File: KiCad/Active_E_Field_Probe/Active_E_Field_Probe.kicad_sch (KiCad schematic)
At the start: 8 parts

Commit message: Something
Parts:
- removed D1: ~, symbol SLiCAP:D
- removed G1: 0.5*s*{C_s}, symbol SLiCAP:G
- removed G2: 2.5*s*{C_s}, symbol SLiCAP:G
- removed H1: 5, symbol SLiCAP:H
- added C1: {0.5*C_s}, symbol SLiCAP:C
- added R1: 50, symbol SLiCAP:R
- R2: noisetemp 0 -> 343
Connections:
- net 0: now also N1.2 (outN)
- net at N1.1 (outP): now also C1.2, R1.1; no longer R2.1
- net at C2.2, N1.3 (inp): now also C1.1
- new net out: R1.2, R2.1
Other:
- moved on the sheet: C2, N1, R2, V1

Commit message: continued work on brute force
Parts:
- R1, R2: noisetemp 343 -> {T_op_max}
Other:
- moved on the sheet: C1, N1
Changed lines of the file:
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@@
 	)
 	(junction
-		(at 123.19 78.74)
+		(at 115.57 78.74)
 		(diameter 0)
 		(color 0 0 0 0)
 	)
 	(junction
-		(at 129.54 78.74)
+		(at 121.92 78.74)
 		(diameter 0)
 		(color 0 0 0 0)
 	)
 	(junction
-		(at 120.65 58.42)
+		(at 113.03 58.42)
 		(diameter 0)
 		(color 0 0 0 0)
 	)
 	(junction
-		(at 130.81 58.42)
+		(at 123.19 58.42)
 		(diameter 0)
 		(color 0 0 0 0)
@@
 	(wire
 		(pts
-			(xy 129.54 73.66) (xy 129.54 78.74)
-		)
-		(stroke
-			(width 0)
-			(type default)
-		)
-	)
-	(wire
-		(pts
-			(xy 120.65 58.42) (xy 123.19 58.42)
-		)
-		(stroke
-			(width 0)
-			(type default)
-		)
-	)
-	(wire
-		(pts
-			(xy 120.65 53.34) (xy 120.65 58.42)
-		)
-		(stroke
-			(width 0)
-			(type default)
-		)
-	)
-	(wire
-		(pts
-			(xy 80.01 78.74) (xy 123.19 78.74)
+			(xy 121.92 73.66) (xy 121.92 78.74)
+		)
+		(stroke
+			(width 0)
+			(type default)
+		)
+	)
+	(wire
+		(pts
+			(xy 113.03 58.42) (xy 115.57 58.42)
+		)
+		(stroke
+			(width 0)
+			(type default)
+		)
+	)
+	(wire
+		(pts
+			(xy 113.03 53.34) (xy 113.03 58.42)
+		)
+		(stroke
+			(width 0)
+			(type default)
+		)
+	)
+	(wire
+		(pts
+			(xy 80.01 78.74) (xy 115.57 78.74)
 		)
 		(stroke
@@
 	(wire
 		(pts
-			(xy 123.19 78.74) (xy 123.19 81.28)
+			(xy 115.57 78.74) (xy 115.57 81.28)
 		)
 		(stroke
@@
 	(wire
 		(pts
-			(xy 130.81 53.34) (xy 130.81 58.42)
+			(xy 123.19 53.34) (xy 123.19 58.42)
 		)
 		(stroke
@@
 	(wire
 		(pts
-			(xy 130.81 58.42) (xy 134.62 58.42)
-		)
-		(stroke
-			(width 0)
-			(type default)
-		)
-	)
-	(wire
-		(pts
-			(xy 80.01 58.42) (xy 120.65 58.42)
+			(xy 123.19 58.42) (xy 134.62 58.42)
+		)
+		(stroke
+			(width 0)
+			(type default)
+		)
+	)
+	(wire
+		(pts
+			(xy 80.01 58.42) (xy 113.03 58.42)
 		)
 		(stroke
@@
 	(wire
 		(pts
-			(xy 129.54 58.42) (xy 130.81 58.42)
+			(xy 121.92 58.42) (xy 123.19 58.42)
 		)
 		(stroke
@@
 	(wire
 		(pts
-			(xy 123.19 63.5) (xy 123.19 58.42)
+			(xy 115.57 63.5) (xy 115.57 58.42)
 		)
 		(stroke
@@
 	(wire
 		(pts
-			(xy 123.19 73.66) (xy 123.19 78.74)
+			(xy 115.57 73.66) (xy 115.57 78.74)
 		)
 		(stroke
@@
 	(wire
 		(pts
-			(xy 129.54 78.74) (xy 148.59 78.74)
-		)
-		(stroke
-			(width 0)
-			(type default)
-		)
-	)
-	(wire
-		(pts
-			(xy 123.19 78.74) (xy 129.54 78.74)
-		)
-		(stroke
-			(width 0)
-			(type default)
-		)
-	)
-	(wire
-		(pts
-			(xy 129.54 58.42) (xy 129.54 63.5)
+			(xy 121.92 78.74) (xy 148.59 78.74)
+		)
+		(stroke
+			(width 0)
+			(type default)
+		)
+	)
+	(wire
+		(pts
+			(xy 115.57 78.74) (xy 121.92 78.74)
+		)
+		(stroke
+			(width 0)
+			(type default)
+		)
+	)
+	(wire
+		(pts
+			(xy 121.92 58.42) (xy 121.92 63.5)
 		)
 		(stroke
@@
 			)
 		)
-		(property "noisetemp" "343"
+		(property "noisetemp" "{T_op_max}"
 			(at 139.7 46.99 90)
 			(show_name yes)
@@
 			)
 		)
-		(property "noisetemp" "343"
+		(property "noisetemp" "{T_op_max}"
 			(at 151.13 67.3099 0)
 			(show_name yes)
@@
 	(symbol
 		(lib_id "SLiCAP:N")
-		(at 129.54 68.58 0)
+		(at 121.92 68.58 0)
 		(unit 1)
 		(exclude_from_sim no)
@@
 		(fields_autoplaced yes)
 		(property "Reference" "N1"
-			(at 132.08 68.5798 0)
+			(at 124.46 68.5798 0)
 			(effects
 				(font
@@
 		)
 		(property "Value" "~"
-			(at 135.89 69.215 0)
+			(at 128.27 69.215 0)
 			(effects
 				(font
@@
 		)
 		(property "Footprint" ""
-			(at 129.54 69.85 0)
+			(at 121.92 69.85 0)
 			(effects
 				(font
@@
 		)
 		(property "Datasheet" ""
-			(at 129.54 69.85 0)
+			(at 121.92 69.85 0)
 			(effects
 				(font
@@
 		)
 		(property "Description" "Nullor"
-			(at 134.62 72.644 0)
+			(at 127 72.644 0)
 			(effects
 				(font
@@
 		)
 		(property "model" "N"
-			(at 131.445 70.485 0)
+			(at 123.825 70.485 0)
 			(show_name yes)
 			(effects
@@
 	(symbol
 		(lib_id "SLiCAP:GND")
-		(at 123.19 81.28 0)
+		(at 115.57 81.28 0)
 		(unit 1)
 		(exclude_from_sim no)
@@
 		(fields_autoplaced yes)
 		(property "Reference" "#01"
-			(at 123.19 86.36 0)
+			(at 115.57 86.36 0)
 			(effects
 				(font
@@
 		)
 		(property "Value" "0"
-			(at 123.19 83.82 0)
+			(at 115.57 83.82 0)
 			(do_not_autoplace yes)
 			(effects
@@
 		)
 		(property "Footprint" ""
-			(at 123.19 81.28 0)
+			(at 115.57 81.28 0)
 			(effects
 				(font
@@
 		)
 		(property "Datasheet" ""
-			(at 123.19 91.44 0)
+			(at 115.57 91.44 0)
 			(effects
 				(font
@@
 		)
 		(property "Description" "0V reference potential"
-			(at 123.19 88.9 0)
+			(at 115.57 88.9 0)
 			(effects
 				(font
@@
 	(symbol
 		(lib_id "SLiCAP:C")
-		(at 125.73 53.34 90)
+		(at 118.11 53.34 90)
 		(unit 1)
 		(exclude_from_sim no)
@@
 		(fields_autoplaced yes)
 		(property "Reference" "C1"
-			(at 125.6637 44.45 90)
+			(at 118.0437 44.45 90)
 			(effects
 				(font
@@
 		)
 		(property "Value" "{0.5*C_s}"
-			(at 125.6637 46.99 90)
+			(at 118.0437 46.99 90)
 			(show_name yes)
 			(effects
@@
 		)
 		(property "Footprint" ""
-			(at 127 50.8 0)
+			(at 119.38 50.8 0)
 			(effects
 				(font
@@
 		)
 		(property "Datasheet" ""
-			(at 127 50.8 0)
+			(at 119.38 50.8 0)
 			(effects
 				(font
@@
 		)
 		(property "Description" "Capacitor"
-			(at 131.826 46.228 0)
+			(at 124.206 46.228 0)
 			(effects
 				(font
@@
 		)
 		(property "model" "C"
-			(at 129.54 50.8 0)
+			(at 121.92 50.8 0)
 			(show_name yes)
 			(effects
@@
 		)
 		(property "vinit" "0"
-			(at 125.6637 49.53 90)
-			(show_name yes)
-			(effects
+			(at 118.0437 49.53 90)
+			(show_name yes)
+			(effects

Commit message: AAAAAAAAAAAHHHHH
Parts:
- removed C1: {0.5*C_s}, symbol SLiCAP:C
- removed C2: {C_s}, symbol SLiCAP:C
- removed N1: ~, symbol SLiCAP:N
- removed R1, R2: 50, symbol SLiCAP:R
- added C3: {C_s}, symbol SLiCAP:C
- added C4: {0.5*C_s}, symbol SLiCAP:C
- added M1, M2: ~, symbol SLiCAP:M
- added R3, R4: 50, symbol SLiCAP:R
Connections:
- net 0: now also M1.3 (S), M1.4 (B), M2.3 (S), M2.4 (B), R4.2
- net out: now also R3.2, R4.1
- net at V1.1 (p): now also C3.1
- new net: C3.2, C4.1, M1.2 (G), M2.2 (G)
- new net LGref: C4.2, M1.1 (D), M2.1 (D), R3.1

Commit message: 01-10 sesh
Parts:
- removed C3: {C_s}, symbol SLiCAP:C
- removed C4: {0.5*C_s}, symbol SLiCAP:C
- removed M1, M2: ~, symbol SLiCAP:M
- removed R3, R4: 50, symbol SLiCAP:R
- added A1, A2, A3: ~, symbol SLiCAP:Command
- added C12: {C_s}, symbol SLiCAP:C
- added C13: {0.5*C_s}, symbol SLiCAP:C
- added R6, R7: 50, symbol SLiCAP:R
- added X1: ~, symbol SLiCAP:XMV
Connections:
- net 0: now also R7.2, X1.3 (S), X1.B (4)
- net out: now also R6.2, R7.1
- net at V1.1 (p): now also C12.1
- new net: C13.2, R6.1, X1.1 (D)
- new net: C12.2, C13.1, X1.2 (G)

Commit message: meeting anton
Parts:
- added A4: ~, symbol SLiCAP:Command
- added X2: ~, symbol SLiCAP:XM

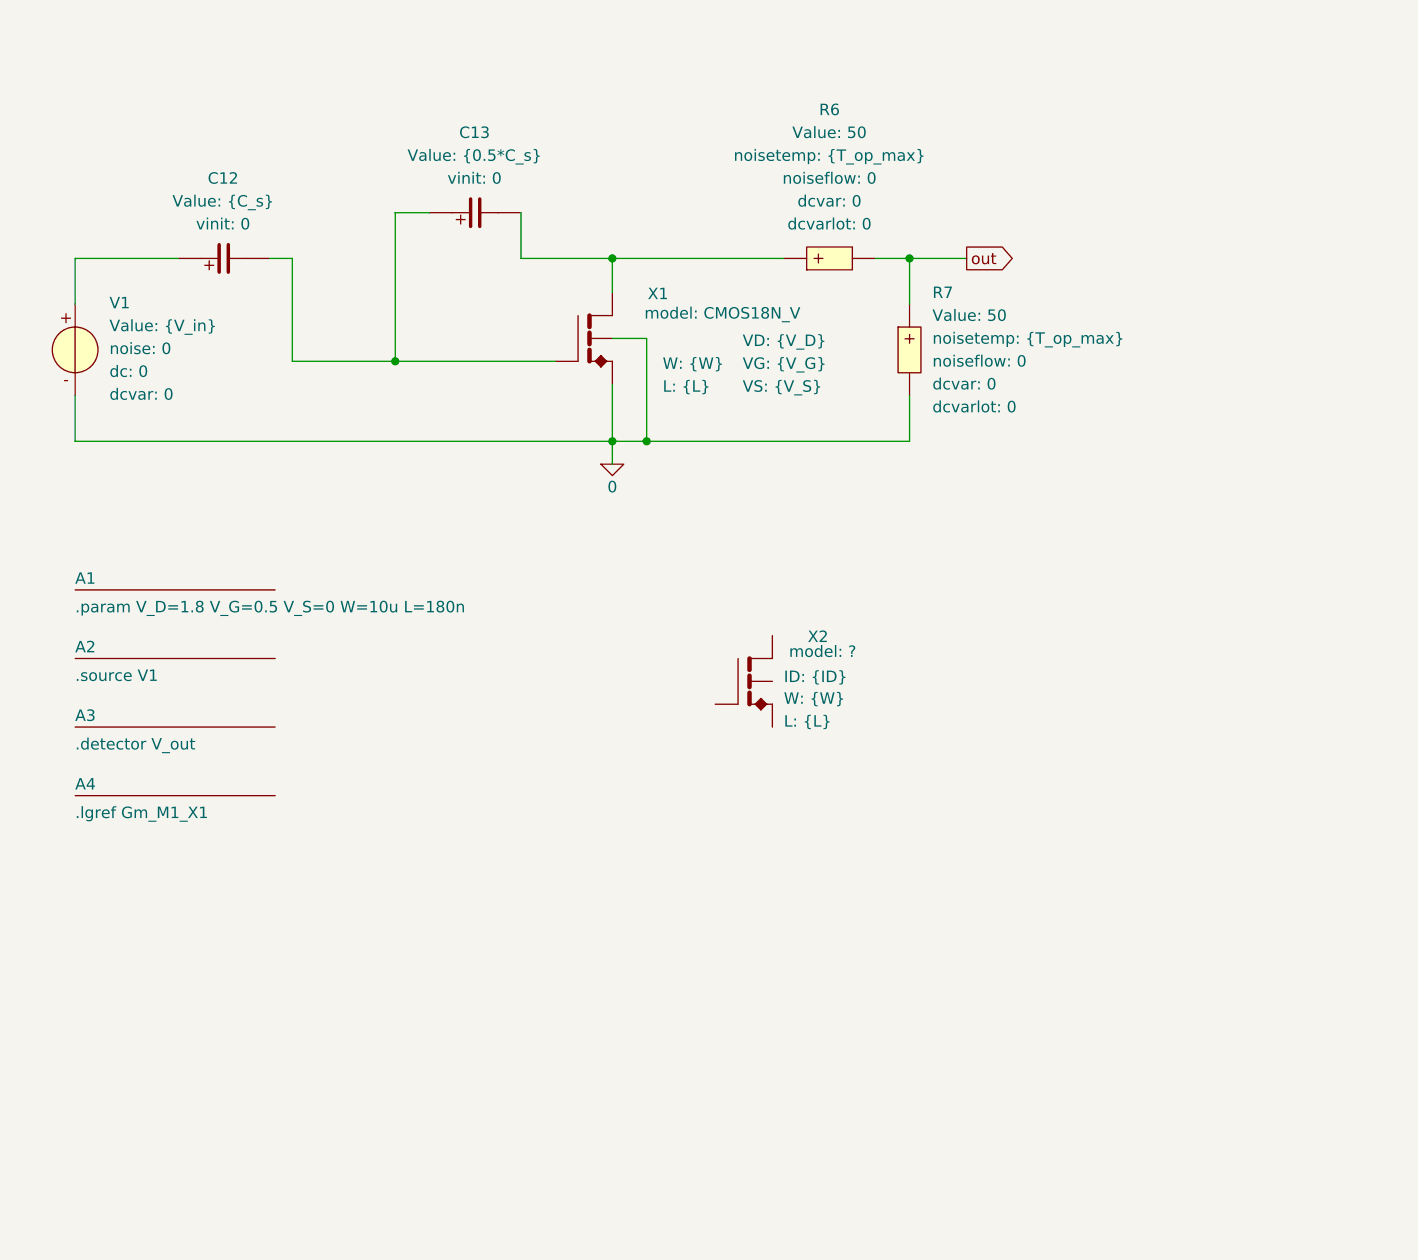
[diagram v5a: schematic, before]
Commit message: Split python files
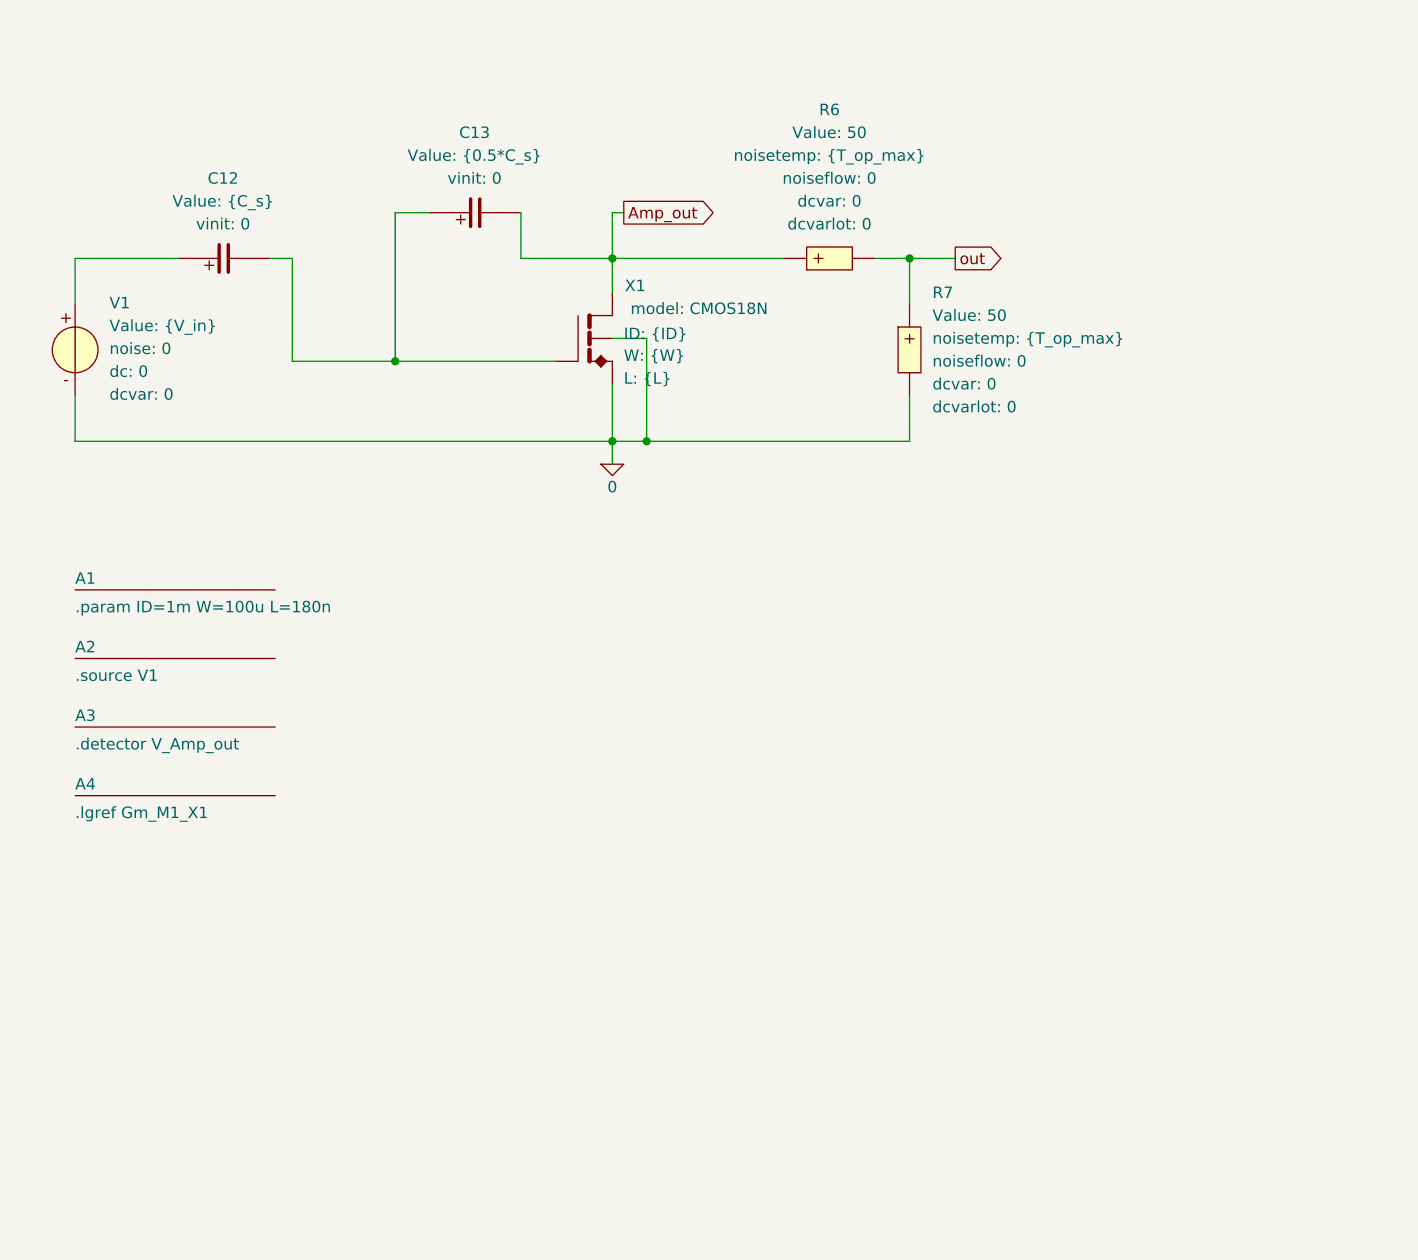
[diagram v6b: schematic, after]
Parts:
- removed X1: ~, symbol SLiCAP:XMV
- removed X2: ~, symbol SLiCAP:XM
- added X1: ~, symbol SLiCAP:XM
- A1: command .param V_D=1.8 V_G=0.5 V_S=0 W=10u L=180n -> .param ID=1m W=100u L=180n
- A3: command .detector V_out -> .detector V_Amp_out
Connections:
- net 0: now also X1.3 (S), X1.4 (B)
- net Amp_out: now reaches C13.2, R6.1
- net Amp_out: now also X1.1 (D)
- net at C12.2, C13.1: now also X1.2 (G)

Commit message: noise stuff
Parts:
- removed A1, A2, A3, A4: ~, symbol SLiCAP:Command
- removed R7: 50, symbol SLiCAP:R
- added I1: 0, symbol SLiCAP:I
- X1: ID {ID} -> {ID_1}; L {L} -> {L_1}; W {W} -> {W_1}
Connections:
- net out is gone; now on net 0: R6.2
- net 0: now also I1.1 (n)
- net Amp_out: now also I1.2 (p)
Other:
- moved on the sheet: C13, R6

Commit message: matrix
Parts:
- removed C12: {C_s}, symbol SLiCAP:C
- removed C13: {0.5*C_s}, symbol SLiCAP:C
- removed I1: 0, symbol SLiCAP:I
- removed R6: 50, symbol SLiCAP:R
- added C14: {C_s}, symbol SLiCAP:C
- added C15: {0.5*C_s}, symbol SLiCAP:C
- added R1, R9: 50, symbol SLiCAP:R
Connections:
- net 0: now also R9.2
- net Amp_out: now also R1.2, R9.1; no longer X1.1 (D)
- net at X1.2 (G): now also C14.2, C15.1
- net at V1.1 (p): now also C14.1
- new net: C15.2, R1.1, X1.1 (D)
